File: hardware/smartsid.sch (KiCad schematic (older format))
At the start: 63 parts, among them P1 INPUT, P2 CONTROL, P4 SOCKET LEFT, P5 OUTPUT, P6 SOCKET RIGHT, Q1 BC547, Q2 BC547, U1 GAL16V8, U2 SID2, U3 7812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

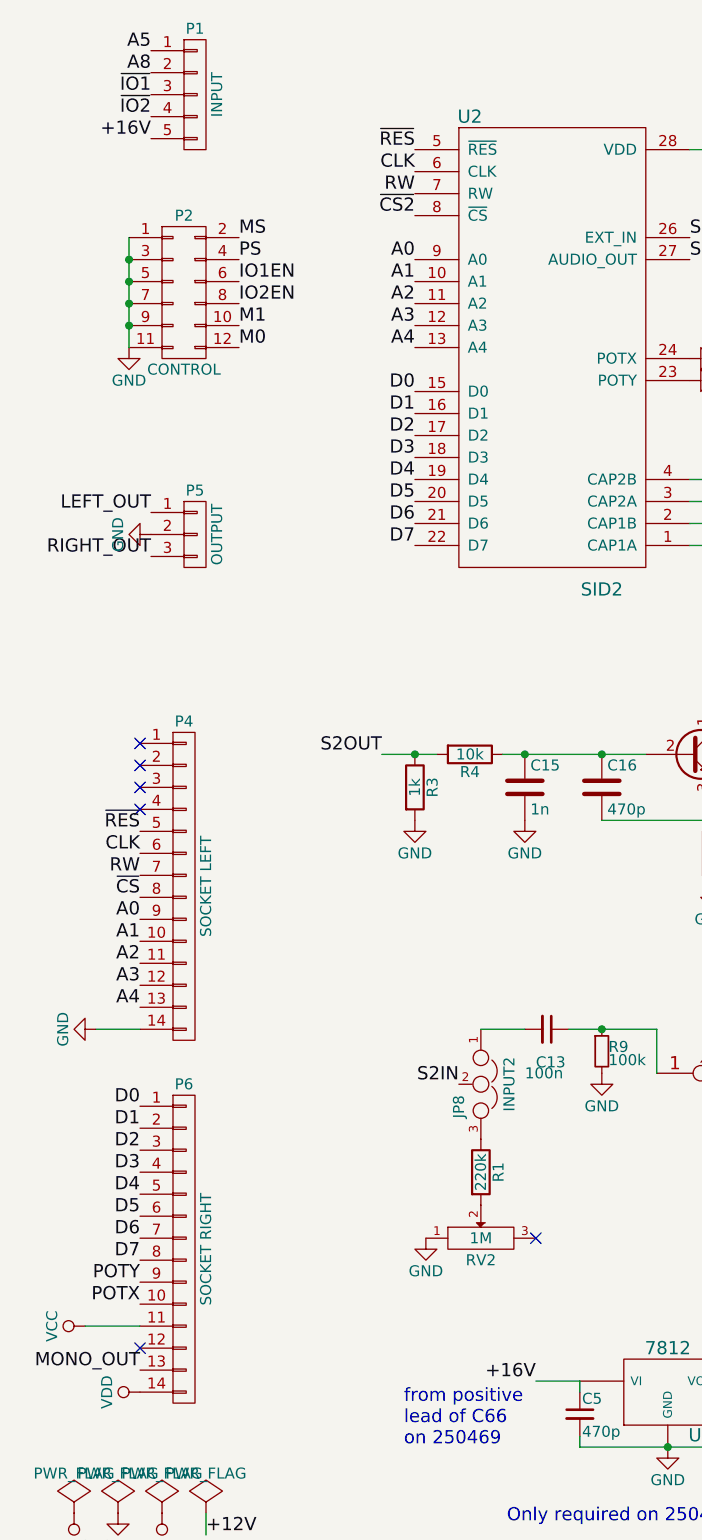
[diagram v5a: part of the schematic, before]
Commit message: Hardware: Renamed +16V line to VEXT, improved silk screen
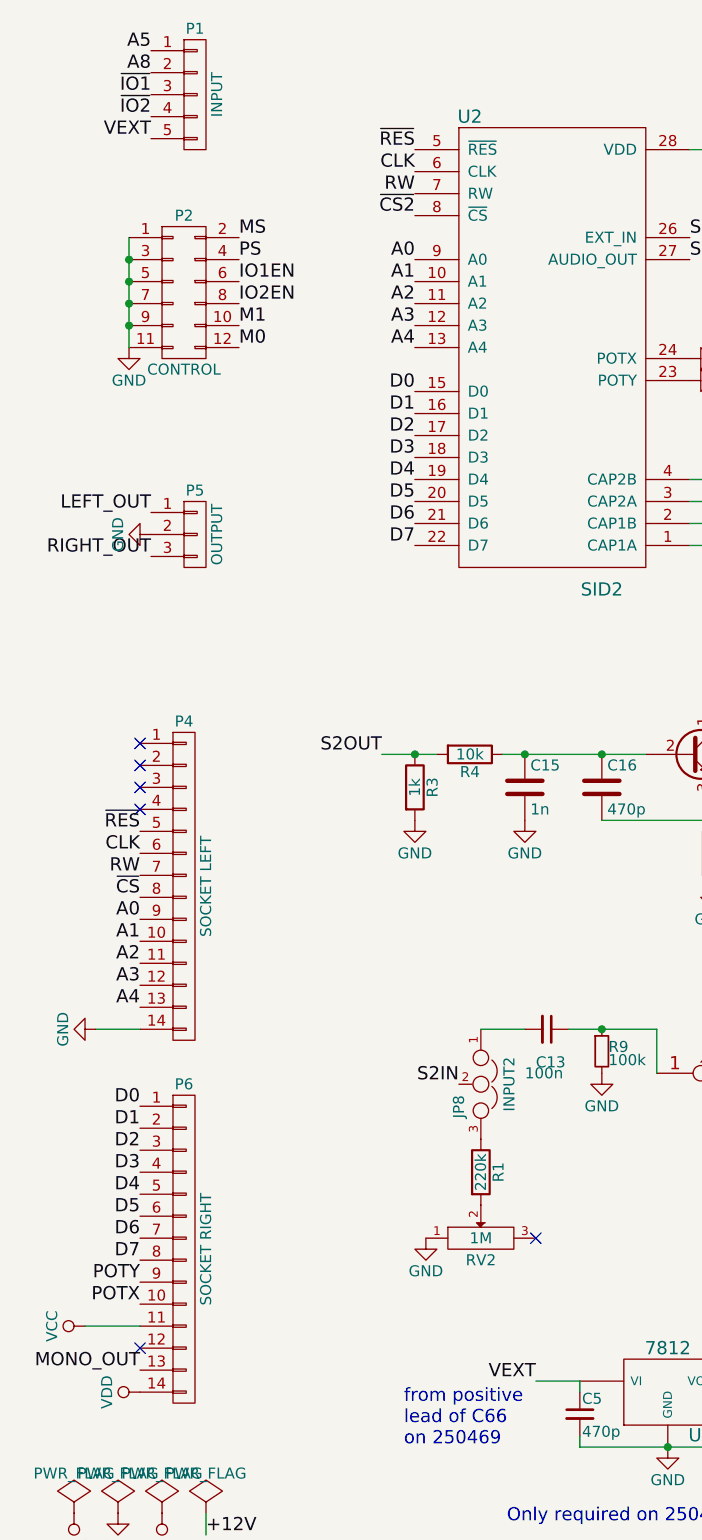
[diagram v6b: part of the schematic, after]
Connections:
- net +16V renamed VEXT
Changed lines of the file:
@@
 $EndComp
 Text Label 2800 6950 2    60   ~ 0
-+16V
+VEXT
 $Comp
 L C_Small C7
@@
 from positive \nlead of C66\non 250469
 Text Label 1050 1300 2    60   ~ 0
-+16V
+VEXT
 Wire Wire Line
 	9800 3250 9800 3350
@@
 PWR1
 $Comp
-L VDD #PWR033
+L VDD #PWR032
 U 1 1 56D9EE0E
 P 4400 6950
-F 0 "#PWR033" H 4400 6800 50  0001 C CNN
+F 0 "#PWR032" H 4400 6800 50  0001 C CNN
 F 1 "VDD" H 4400 7100 50  0000 C CNN
 F 2 "" H 4400 6950 60  0000 C CNN
@@
 $EndComp
 $Comp
-L PWR_FLAG #FLG034
+L PWR_FLAG #FLG033
 U 1 1 56D9EC00
 P 1100 7550
-F 0 "#FLG034" H 1100 7645 50  0001 C CNN
+F 0 "#FLG033" H 1100 7645 50  0001 C CNN
 F 1 "PWR_FLAG" H 1100 7730 50  0000 C CNN
 F 2 "" H 1100 7550 60  0000 C CNN
@@
 $EndComp
 $Comp
-L VDD #PWR035
+L VDD #PWR034
 U 1 1 56D9EC5F
 P 1100 7550
-F 0 "#PWR035" H 1100 7400 50  0001 C CNN
+F 0 "#PWR034" H 1100 7400 50  0001 C CNN
 F 1 "VDD" H 1100 7700 50  0000 C CNN
 F 2 "" H 1100 7550 60  0000 C CNN
@@
 	6900 4450 7000 4450
 $Comp
-L GND #PWR?
+L GND #PWR035
 U 1 1 570B5EB9
 P 3500 2300
-F 0 "#PWR?" H 3500 2050 50  0001 C CNN
+F 0 "#PWR035" H 3500 2050 50  0001 C CNN
 F 1 "GND" H 3500 2150 50  0000 C CNN
 F 2 "" H 3500 2300 60  0000 C CNN
@@
 $EndComp
 $Comp
-L GND #PWR?
+L GND #PWR036
 U 1 1 570B5F8B
 P 3500 2400
-F 0 "#PWR?" H 3500 2150 50  0001 C CNN
+F 0 "#PWR036" H 3500 2150 50  0001 C CNN
 F 1 "GND" H 3500 2250 50  0000 C CNN
 F 2 "" H 3500 2400 60  0000 C CNN

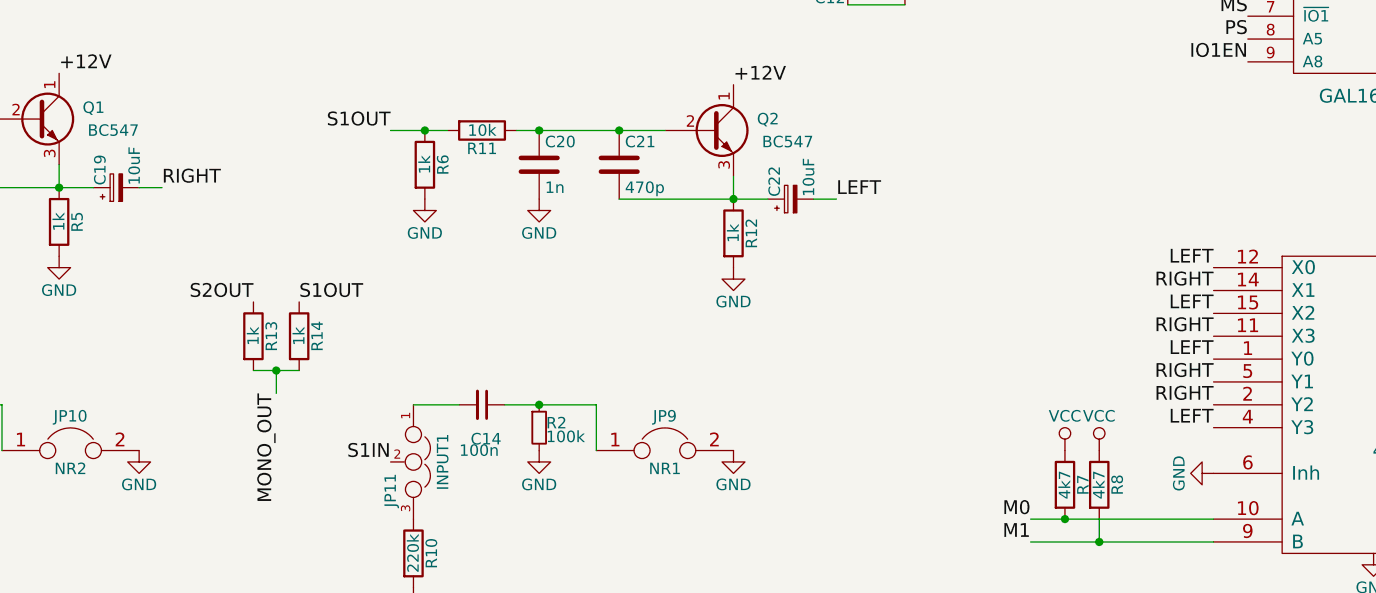
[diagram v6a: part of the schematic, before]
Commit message: Hardware: Corrected order of SIDs on audio channels, default mix setting
Now the left sid appears on the left channel and the right sid on the right
channel. Also the default mix state (without driving M0 and M1) has been
changed to Left/Right. This should match expectations.
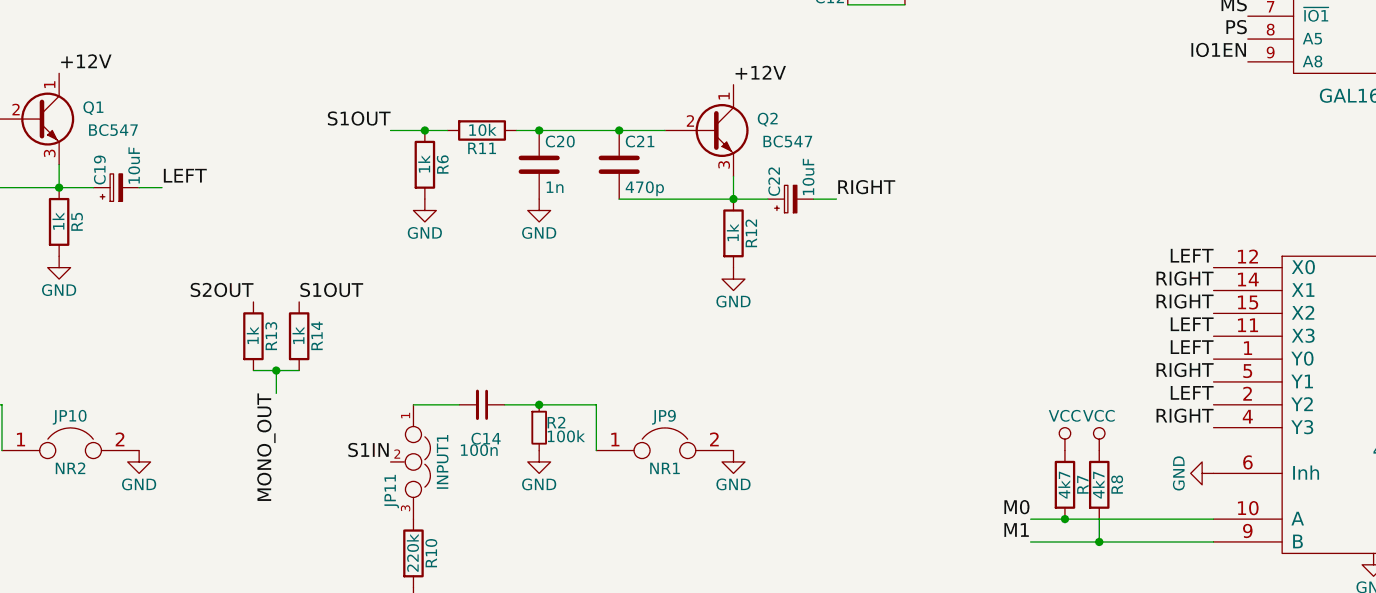
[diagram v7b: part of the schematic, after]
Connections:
- net LEFT: now also C19.2, U6.11 (X3), U6.2 (Y2); no longer C22.2, U6.15 (X2), U6.4 (Y3)
- net RIGHT: now also C22.2, U6.15 (X2), U6.4 (Y3); no longer C19.2, U6.11 (X3), U6.2 (Y2)
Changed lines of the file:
@@
 	0    1    1    0
 $EndComp
+Text Label 7000 4450 0    60   ~ 0
+RIGHT
 Text Label 4050 4400 0    60   ~ 0
-RIGHT
-Text Label 7000 4450 0    60   ~ 0
 LEFT
 $Comp
@@
 Text Label 8650 5250 2    60   ~ 0
 RIGHT
+Text Label 8650 5050 2    60   ~ 0
+LEFT
+Text Label 8650 5450 2    60   ~ 0
+RIGHT
 Text Label 8650 4950 2    60   ~ 0
-LEFT
+RIGHT
 Text Label 8650 5350 2    60   ~ 0
-RIGHT
-Text Label 8650 5050 2    60   ~ 0
-RIGHT
-Text Label 8650 5450 2    60   ~ 0
 LEFT
 Text Label 1050 3000 2    60   ~ 0

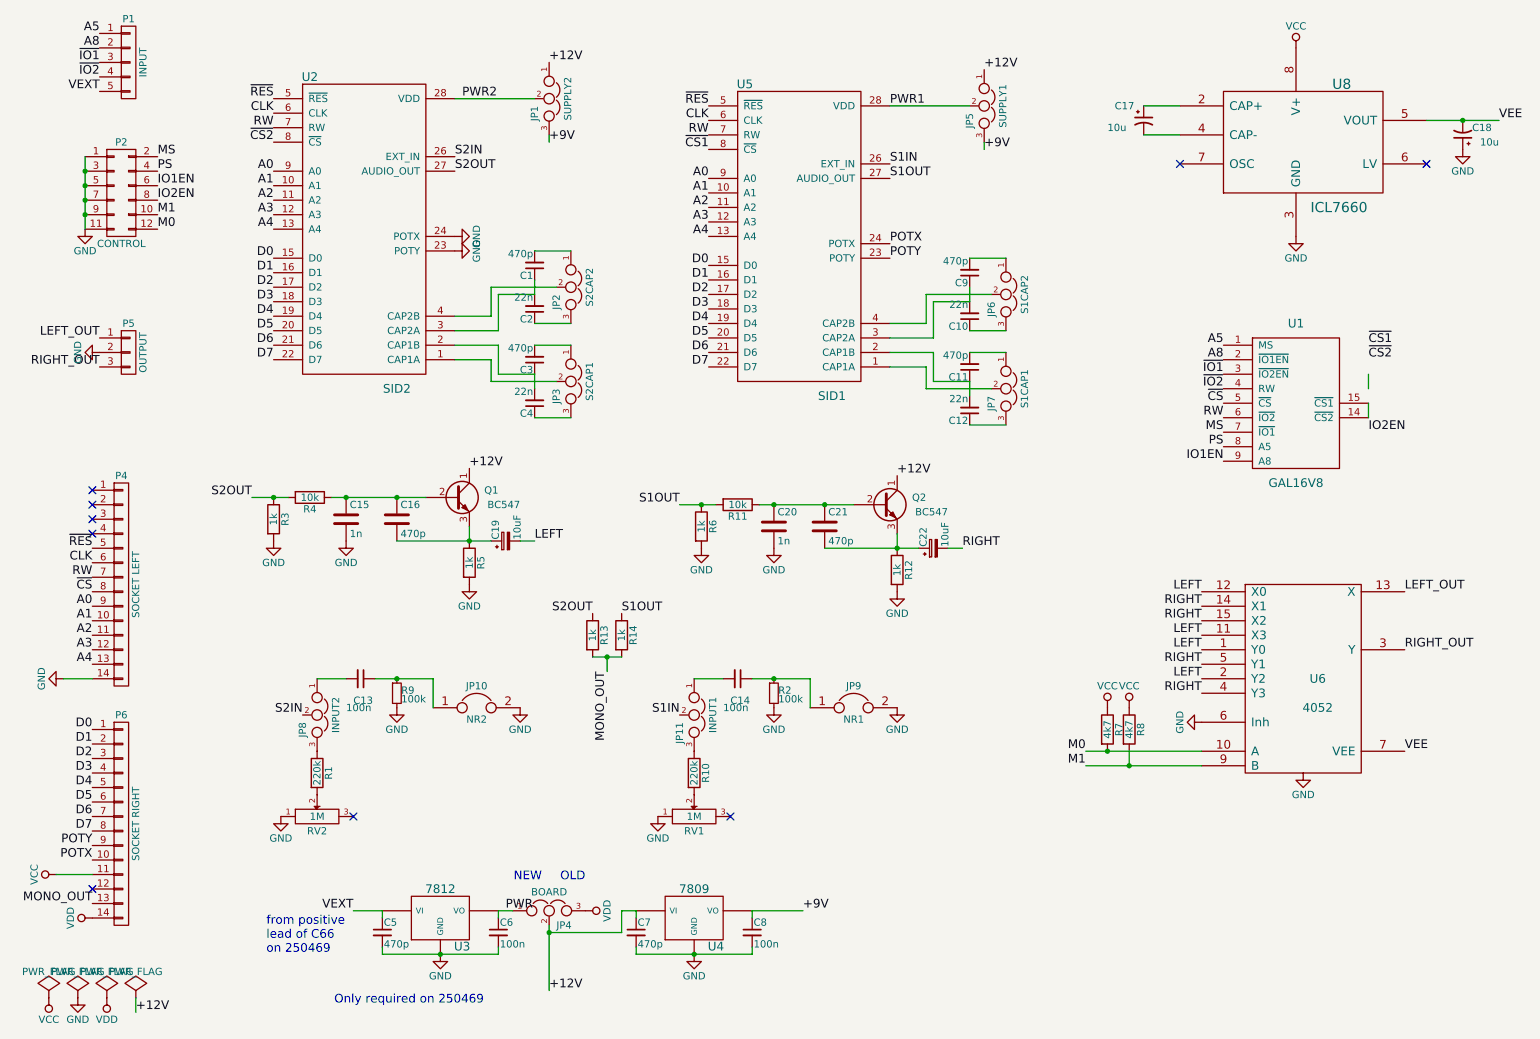
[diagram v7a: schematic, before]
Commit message: Hardware: Removed priority select, rearranged GAL pin layout
Switching SID priorities does not seem very useful and will break paddles
when priority is swapped in stereo addressing mode.
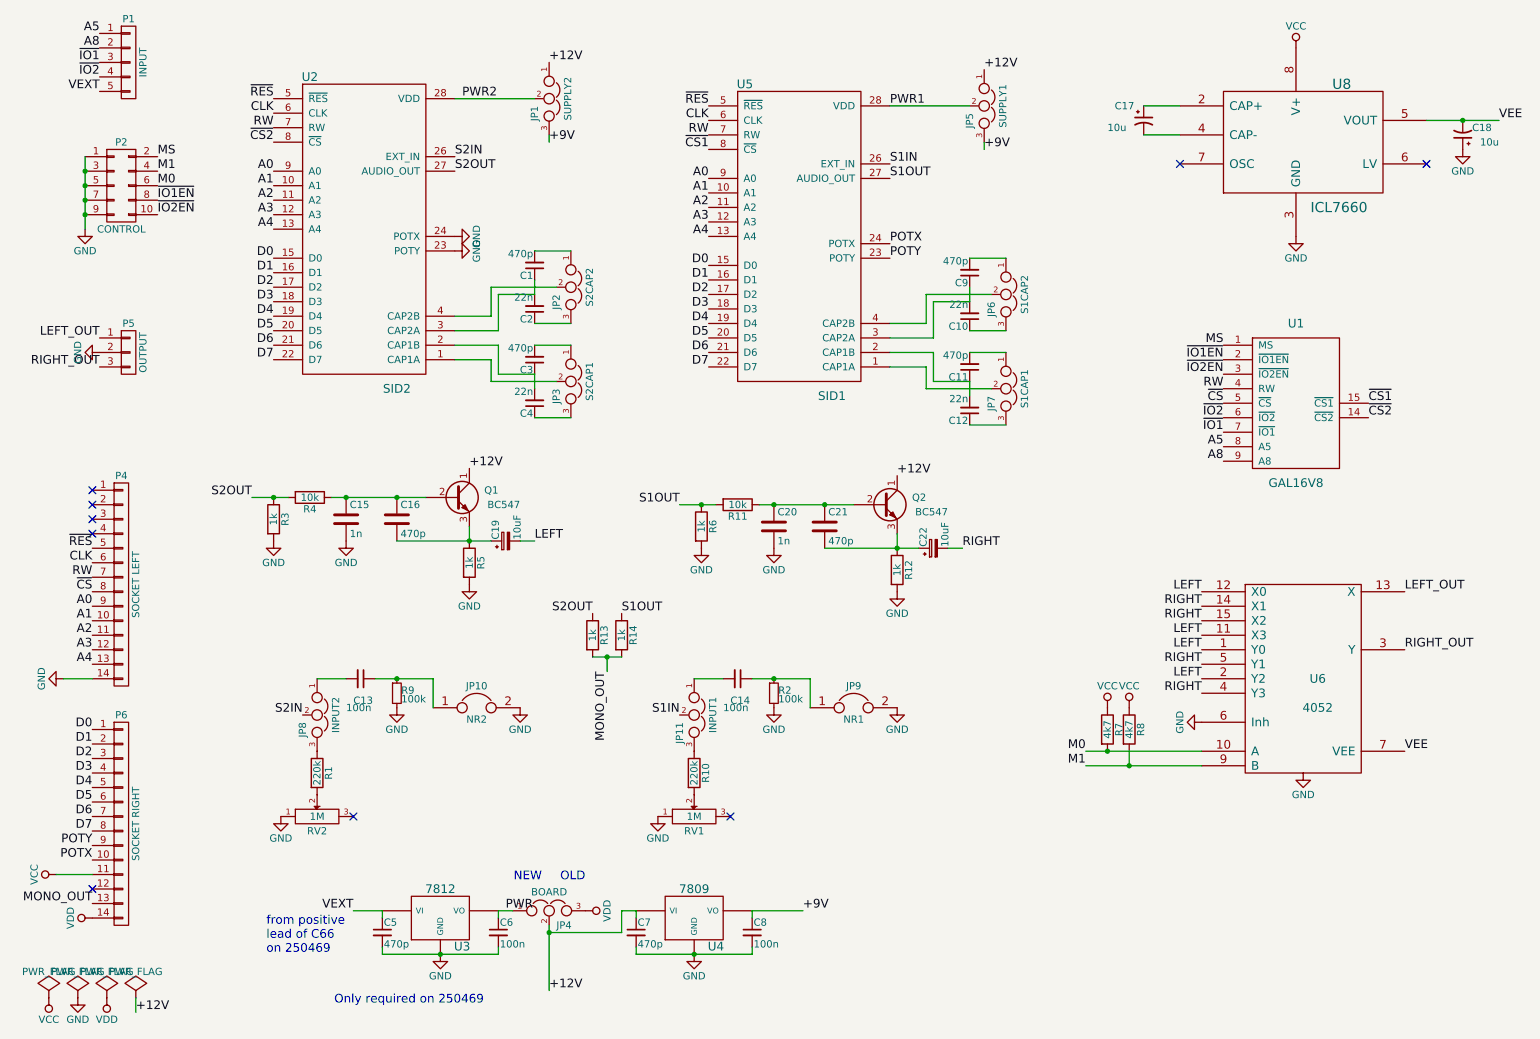
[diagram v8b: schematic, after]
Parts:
- removed P2: CONTROL, Pinheaders:Pin_Header_Straight_2x06, symbol CONN_02X06
- added P2: CONTROL, Pin_Headers:Pin_Header_Straight_2x05, symbol CONN_02X05
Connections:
- net IO1EN is gone; now on net A8: U1.9 (A8)
- net PS is gone; now on net A5: U1.8 (A5)
- net A5: no longer U1.1 (MS)
- net A8: no longer U1.2 (~IO1EN)
- net GND: now also P2.1 (P1), P2.3 (P3), P2.5 (P5), P2.7 (P7), P2.9 (P9)
- net M0: now also P2.6 (P6)
- net M1: now also P2.4 (P4)
- net MS: now also U1.1 (MS), P2.2 (P2); no longer U1.7 (~IO1)
- net RW: now also U1.4 (RW); no longer U1.6 (~IO2)
- net ~CS1: now also U1.15 (~CS1); no longer U1.19 (NC)
- net ~CS2: now also U1.14 (~CS2); no longer U1.18 (NC)
- net ~IO1: now also U1.7 (~IO1); no longer U1.3 (~IO2EN)
- net ~IO2: now also U1.6 (~IO2); no longer U1.4 (RW)
- net at U1.16 (NC): no longer U1.17 (NC)
- net IO2EN: no longer names the net of U1.13 (NC)
- new net ~IO1EN: P2.8 (P8), U1.2 (~IO1EN)
- new net ~IO2EN: P2.10 (P10), U1.3 (~IO2EN)
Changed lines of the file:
@@
-	1    0    0    -1
-$EndComp
-$Comp
-L SMARTSID U1
-U 1 1 56D81BBF
-P 9300 3450
-F 0 "U1" H 9300 4000 60  0000 C CNN
-F 1 "GAL16V8" H 9300 2900 60  0000 C CNN
-F 2 "Housings_DIP:DIP-20_W7.62mm" H 9350 3200 60  0001 C CNN
-F 3 "" H 9350 3200 60  0000 C CNN
-	1    9300 3450
 	1    0    0    -1
 $EndComp
@@
 Text Label 1050 1200 2    60   ~ 0
 ~IO2
-Text Label 8800 3050 2    60   ~ 0
+Text Label 8800 3750 2    60   ~ 0
 A5
-Text Label 8800 3150 2    60   ~ 0
+Text Label 8800 3850 2    60   ~ 0
 A8
-Text Label 8800 3250 2    60   ~ 0
+Text Label 8800 3650 2    60   ~ 0
 ~IO1
-Text Label 8800 3350 2    60   ~ 0
+Text Label 8800 3550 2    60   ~ 0
 ~IO2
 $Comp
@@
 Text Label 8800 3450 2    60   ~ 0
 ~CS
-Text Label 9800 3050 0    60   ~ 0
+Text Label 9800 3450 0    60   ~ 0
 ~CS1
-Text Label 9800 3150 0    60   ~ 0
+Text Label 9800 3550 0    60   ~ 0
 ~CS2
 Text Label 5250 1700 2    60   ~ 0
@@
 Text Label 6500 2450 0    60   ~ 0
 POTY
-Text Label 8800 3550 2    60   ~ 0
+Text Label 8800 3350 2    60   ~ 0
 RW
-Text Label 8800 3650 2    60   ~ 0
+Text Label 8800 3050 2    60   ~ 0
 MS
-Text Label 8800 3750 2    60   ~ 0
-PS
-Text Label 8800 3850 2    60   ~ 0
-IO1EN
+Text Label 8800 3150 2    60   ~ 0
+~IO1EN
 Text Label 1450 1750 0    60   ~ 0
 MS
-Text Label 1450 1850 0    60   ~ 0
-PS
-Text Label 1450 1950 0    60   ~ 0
-IO1EN
+Text Label 1450 2050 0    60   ~ 0
+~IO1EN
 $Comp
 L JUMPER3 JP2
@@
 Text Label 10050 5150 0    60   ~ 0
 RIGHT_OUT
-Text Label 1450 2250 0    60   ~ 0
+Text Label 1450 1950 0    60   ~ 0
 M0
-Text Label 1450 2150 0    60   ~ 0
+Text Label 1450 1850 0    60   ~ 0
 M1
 Text Notes 3700 7600 2    60   ~ 0
@@
 VEXT
 Wire Wire Line
-	9800 3250 9800 3350
-Wire Wire Line
-	9800 3450 9800 3550
-Wire Wire Line
 	4050 2400 4300 2400
 Wire Wire Line
@@
 Wire Wire Line
 	4650 6950 4750 6950
-Text Label 1450 2050 0    60   ~ 0
-IO2EN
-Text Label 9800 3650 0    60   ~ 0
-IO2EN
+Text Label 1450 2150 0    60   ~ 0
+~IO2EN
+Text Label 8800 3250 2    60   ~ 0
+~IO2EN
 $Comp
 L ICL7660 U8
@@
 $EndComp
 $Comp
-L CONN_02X06 P2
-U 1 1 56EAD3D7
-P 1200 2000
-F 0 "P2" H 1200 2350 50  0000 C CNN
-F 1 "CONTROL" H 1200 1650 50  0000 C CNN
-F 2 "Pinheaders:Pin_Header_Straight_2x06" H 1200 800 60  0001 C CNN
-F 3 "" H 1200 800 60  0000 C CNN
-	1    1200 2000
-	1    0    0    -1
-$EndComp
-$Comp
 L GND #PWR031
 U 1 1 56EAEE9D
@@
 	0    -1   -1   0
 $EndComp
+$Comp
+L CONN_02X05 P2
+U 1 1 570C5ED8
+P 1200 1950
+F 0 "P2" H 1200 2250 50  0000 C CNN
+F 1 "CONTROL" H 1200 1650 50  0000 C CNN
+F 2 "Pin_Headers:Pin_Header_Straight_2x05" H 1200 750 60  0001 C CNN
+F 3 "" H 1200 750 60  0000 C CNN
+	1    1200 1950
+	1    0    0    -1
+$EndComp
+$Comp
+L SMARTSID U1
+U 1 1 56D81BBF
+P 9300 3450
+F 0 "U1" H 9300 4000 60  0000 C CNN
+F 1 "GAL16V8" H 9300 2900 60  0000 C CNN
+F 2 "Housings_DIP:DIP-20_W7.62mm" H 9350 3200 60  0001 C CNN
+F 3 "" H 9350 3200 60  0000 C CNN
+	1    9300 3450
+	1    0    0    -1
+$EndComp
 $EndSCHEMATC
